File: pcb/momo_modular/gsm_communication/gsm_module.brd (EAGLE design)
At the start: 67.5 x 30.5 mm, 21 parts, among them U10 ESD-SMF05C

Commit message: Finalized the following boards for fabrication/assembly: Sensor Dev Board GSM Module Combined Wallpower and Controller Boards
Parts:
- removed U$7, U$8: BUFFER-OD, components:SC70-5L
- added JP2: (no value), pinhead:1X03
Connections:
- removed net LINE1: U$2.6, U$8.2
- removed net N$6: U$6.15, U$7.5, U$8.5
- removed net N$8: U$2.5, U$7.2
- new net DEBUGRX: JP2.2, U$6.28
- new net DEBUGTX: JP2.1, U$6.27
- new net VDD_EXT: U$6.15
- net GND: now also JP2.3; no longer U$7.3, U$8.3
- net PWRKEY: now also U$2.5; no longer U$7.4
- net RESET: now also U$2.6; no longer U$8.4
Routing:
- net PWRKEY: track 20.4 -> 77.0 mm
- net LINE1: track 56.4 -> 0.00 mm
- net N$8: track 53.5 -> 0.00 mm
- net RESET: track 7.95 -> 60.7 mm, vias 0 -> 2
- net DEBUGRX: track 0.00 -> 22.5 mm
- net DEBUGTX: track 0.00 -> 20.6 mm
- net N$6: track 11.8 -> 0.00 mm
- net GND: track 320.0 -> 320.1 mm, vias 84 -> 83
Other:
- board size 67.5 x 30.5 mm -> 68.6 x 33 mm
- board text added: "GND"
- board text added: "RX"
- board text added: "TX"
- board text added: "U$1"

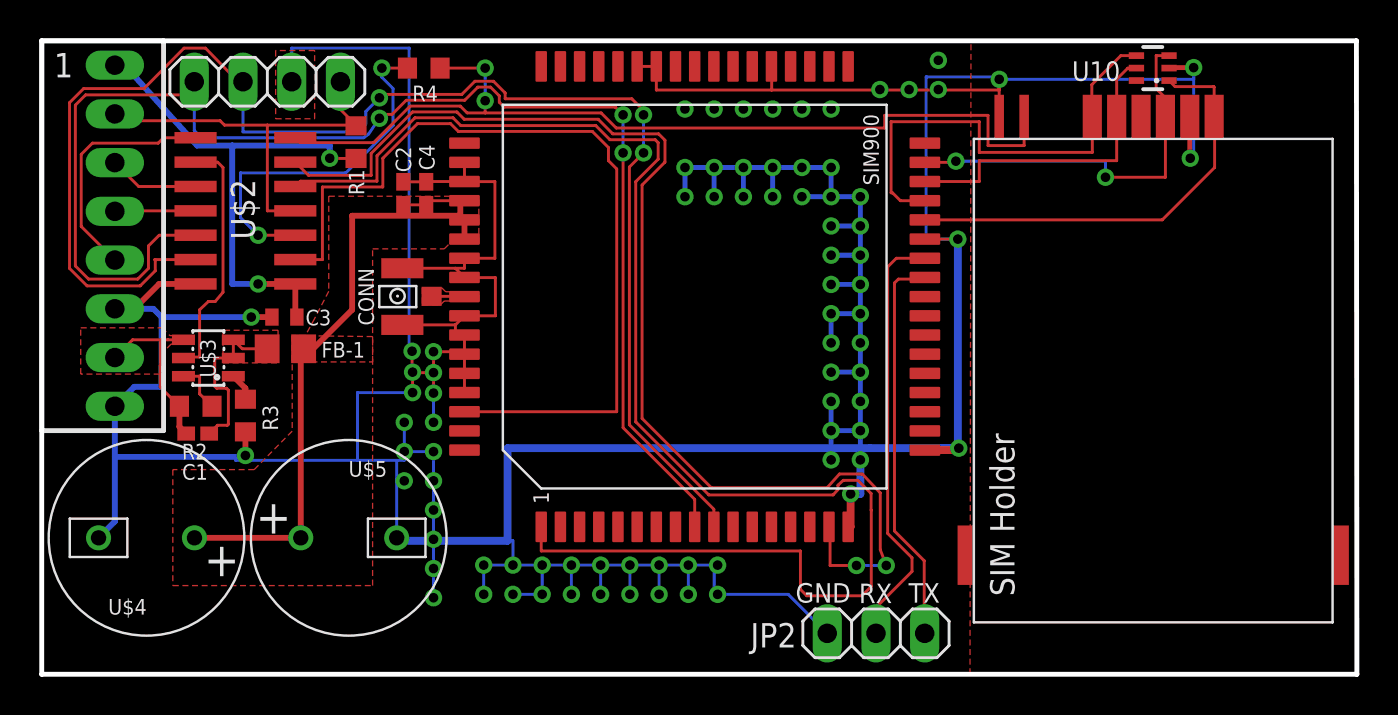
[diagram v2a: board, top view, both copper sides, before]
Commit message: Finished next version of hardware.  Working on automatic BOM generation for purchasing.
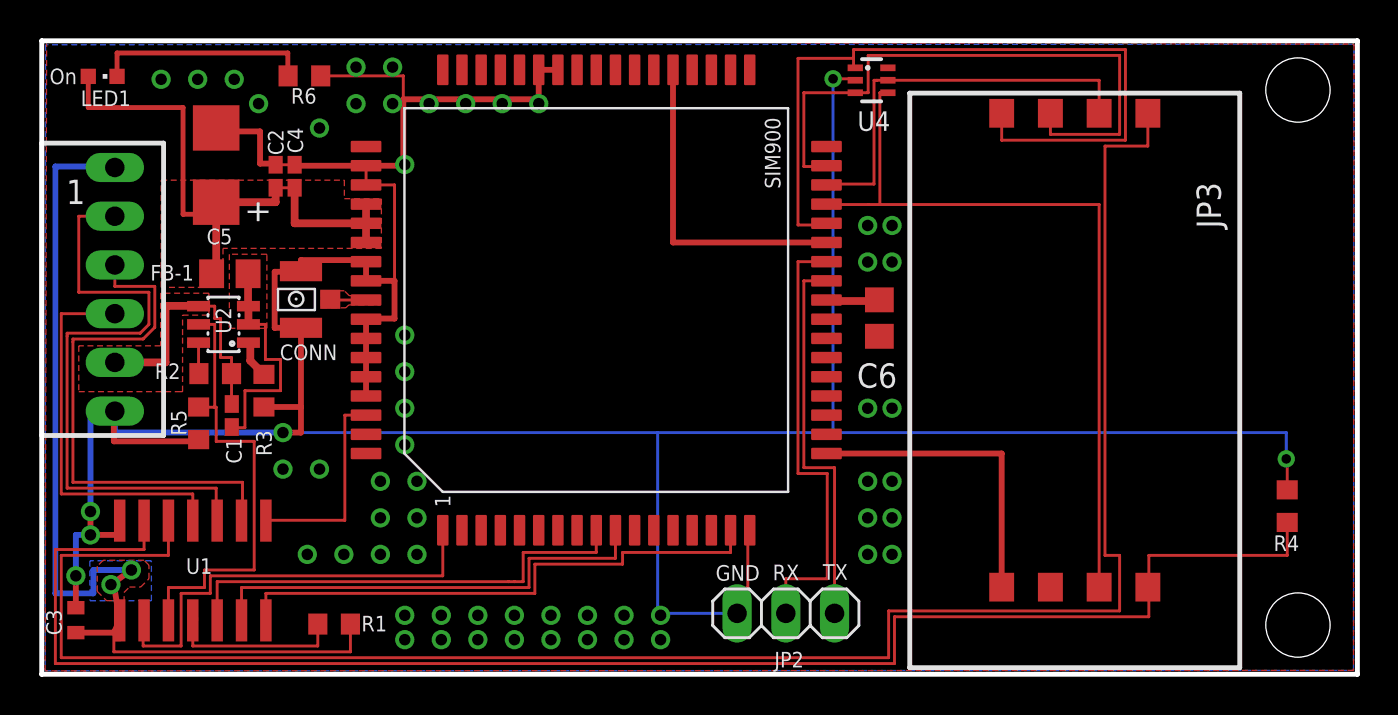
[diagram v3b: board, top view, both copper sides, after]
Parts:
- removed U$1: MOMO-EDGE-8M, components:MOMO-EDGE-8M
- removed U$2: PIC16LF1823, components:SO14
- removed U$3: TI-HIGHSIDE-PFET, components:SOT23-6L
- removed U$4, U$5: 2200uF, components:CAP-10MM
- removed U$6: SIM900, components:SIM900
- removed U$9: SIMHOLDER-8PIN, components:SIMHOLDER-WITH-SWITCH
- removed U10: ESD-SMF05C, components:SC70-6L
- added C5: 330 uF, components:2917
- added C6: 4.7 uF, rcl:C0805
- added JP3: SIMHOLDER-8PINHING, components:CCM03-SIMHOLDER
- added LED1: (no value), led:CHIPLED_0603
- added R5: 100K, rcl:R0603
- added R6: 470R, rcl:R0603
- added U1: PIC16LF1823, components:SO14
- added U2: TI-HIGHSIDE-PFET, components:SOT23-6L
- added U3: SIM900, components:SIM900
- added U4: ESD-SMF05C, components:SC70-6L
- JP1: value (none) -> MOMO-EDGE-6M; device pinhead:1X04 -> components:MOMO-EDGE-6M
- R2: value 25K -> 15K
- R3: value 2.5K -> 1.5K
- moved R4 50.5 mm to (70.0, 13.8), turned to 270 degrees
- moved R1 25.1 mm to (20.3, 7.70), turned to 0 degrees
- moved C3 19.2 mm to (6.86, 7.90), turned to 90 degrees
- moved JP1 16.7 mm to (8.89, 21.3)
- moved C4 6.92 mm to (18.3, 31.0)
- moved C2 6.71 mm to (17.3, 31.0)
- moved CONN 5.29 mm to (17.3, 23.1)
- moved FB-1 4.87 mm to (14.9, 26.0), turned to 180 degrees
- moved JP2 4.81 mm to (43.9, 8.26)
- moved C1 2.01 mm to (15.0, 18.6), turned to 90 degrees
- moved R2 1.98 mm to (14.1, 20.8), turned to 0 degrees
- moved R3 1.62 mm to (16.7, 19.9)
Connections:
- removed net ICLK: JP1.1, U$2.12, U$6.9
- removed net IDAT: JP1.2, U$2.13, U$6.10
- removed net PMCLR: JP1.4, R1.1, U$1.NC, U$2.4
- removed net SIMSW1: R4.1, U$2.7, U$9.SW1
- removed net VRTC: U$6.26
- new net N$5: C6.1, U3.26
- new net N$6: R1.1, U1.4
- new net RXD: U1.6, U3.10
- new net SW1: JP3.SW1, U1.12
- new net SW2: JP3.SW2, R4.2, U1.13
- new net TXD: U1.5, U3.9
- net ALARM: now also JP1.ALARM, U1.11; no longer U$1.ALRM, U$2.8
- net CLOCK: now also JP1.CLK, U1.10; no longer U$1.CLK, U$2.10
- net DAT: now also JP1.DAT, U1.9; no longer U$1.DAT, U$2.11
- net DEBUGRX: now also U3.28; no longer U$6.28
- net DEBUGTX: now also U3.27; no longer U$6.27
- net GND: now also C5.-, C6.2, JP1.GND, JP3.GND, R4.1, R5.1, R6.1, U1.14, U3.17, U3.18, U3.29, U3.39, U3.45, U3.46, U3.53, U3.54, U3.58, U3.59, U3.61, U3.62, U3.63, U3.64, U3.65, U4.2; no longer JP1.3, U$1.GND, U$1.PGND, U$2.14, U$4.-, U$5.-, U$6.17, U$6.18, U$6.29, U$6.39, U$6.45, U$6.46, U$6.53, U$6.54, U$6.58, U$6.59, U$6.61, U$6.62, U$6.63, U$6.64, U$6.65, U$9.GND, U$9.SW2, U10.2
- net N$1: now also U2.1; no longer U$3.1
- net N$2: now also LED1.C, R6.2; no longer R4.2, U$2.3
- net N$3: now also U2.6; no longer U$3.6
- net N$4: now also U2.2, U2.3; no longer U$3.2, U$3.3
- net N$7: now also U3.60; no longer U$6.60
- net POW-SW-ON: now also R5.2, U1.3, U2.5; no longer U$2.9, U$3.5
- net PWRKEY: now also U1.2, U3.1; no longer U$2.5, U$6.1
- net RESET: now also U1.7, U3.16; no longer U$2.6, U$6.16
- net SIMCLK: now also JP3.CLOCK, U3.32, U4.5; no longer U$6.32, U$9.SIMCLK, U10.5
- net SIMDAT: now also JP3.IO, U3.31, U4.4; no longer U$6.31, U$9.SIMIO, U10.4
- net SIMRST: now also JP3.RESET, U3.33, U4.3; no longer U$6.33, U$9.SIMRST, U10.3
- net SIMVCC: now also JP3.VCC, U3.30, U4.1; no longer U$6.30, U$9.SIMVCC, U10.1
- net STATUS: now also U1.8, U3.66; no longer U$2.2, U$6.66
- net V+: now also JP1.4V, U2.4; no longer U$1.V4, U$3.4
- net VCCINT: now also JP1.V28, U1.1; no longer U$1.V28, U$2.1
- net VDD: now also C5.+, LED1.A, U3.55, U3.56, U3.57; no longer U$4.+, U$5.+, U$6.55, U$6.56, U$6.57
- net VDD_EXT: now also U3.15; no longer U$6.15
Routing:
- net SW1: track 0.00 -> 99.3 mm
- net GND: track 320.1 -> 223.1 mm, vias 83 -> 62
- net SW2: track 0.00 -> 83.7 mm
- net IDAT: track 77.2 -> 0.00 mm, vias 3 -> 0
- net ICLK: track 73.3 -> 0.00 mm, vias 3 -> 0
- net PWRKEY: track 77.0 -> 23.0 mm
- net SIMSW1: track 47.8 -> 0.00 mm, vias 2 -> 0
- net STATUS: track 44.8 -> 10.7 mm
- net RESET: track 60.7 -> 28.9 mm, vias 2 -> 0
- net CLOCK: track 4.72 -> 33.2 mm
- net TXD: track 0.00 -> 24.5 mm
- net RXD: track 0.00 -> 24.2 mm
- net VCCINT: track 27.4 -> 51.4 mm
- net DAT: track 4.22 -> 28.2 mm
- net PMCLR: track 21.4 -> 0.00 mm
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- added copper zone on layer 1, net VCCINT
- added copper zone on layer 16, net VCCINT
- removed copper zone on layer 1, net N$2
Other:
- outline, holes or cut-outs redrawn
- board text added: "On"
- board text removed: "U$1"
